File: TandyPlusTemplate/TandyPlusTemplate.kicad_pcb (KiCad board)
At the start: 2 copper layers, 3 parts, among them J1 Input BUS, J2 Passthrough Bus Short, J3 Passthrough Bus Tall

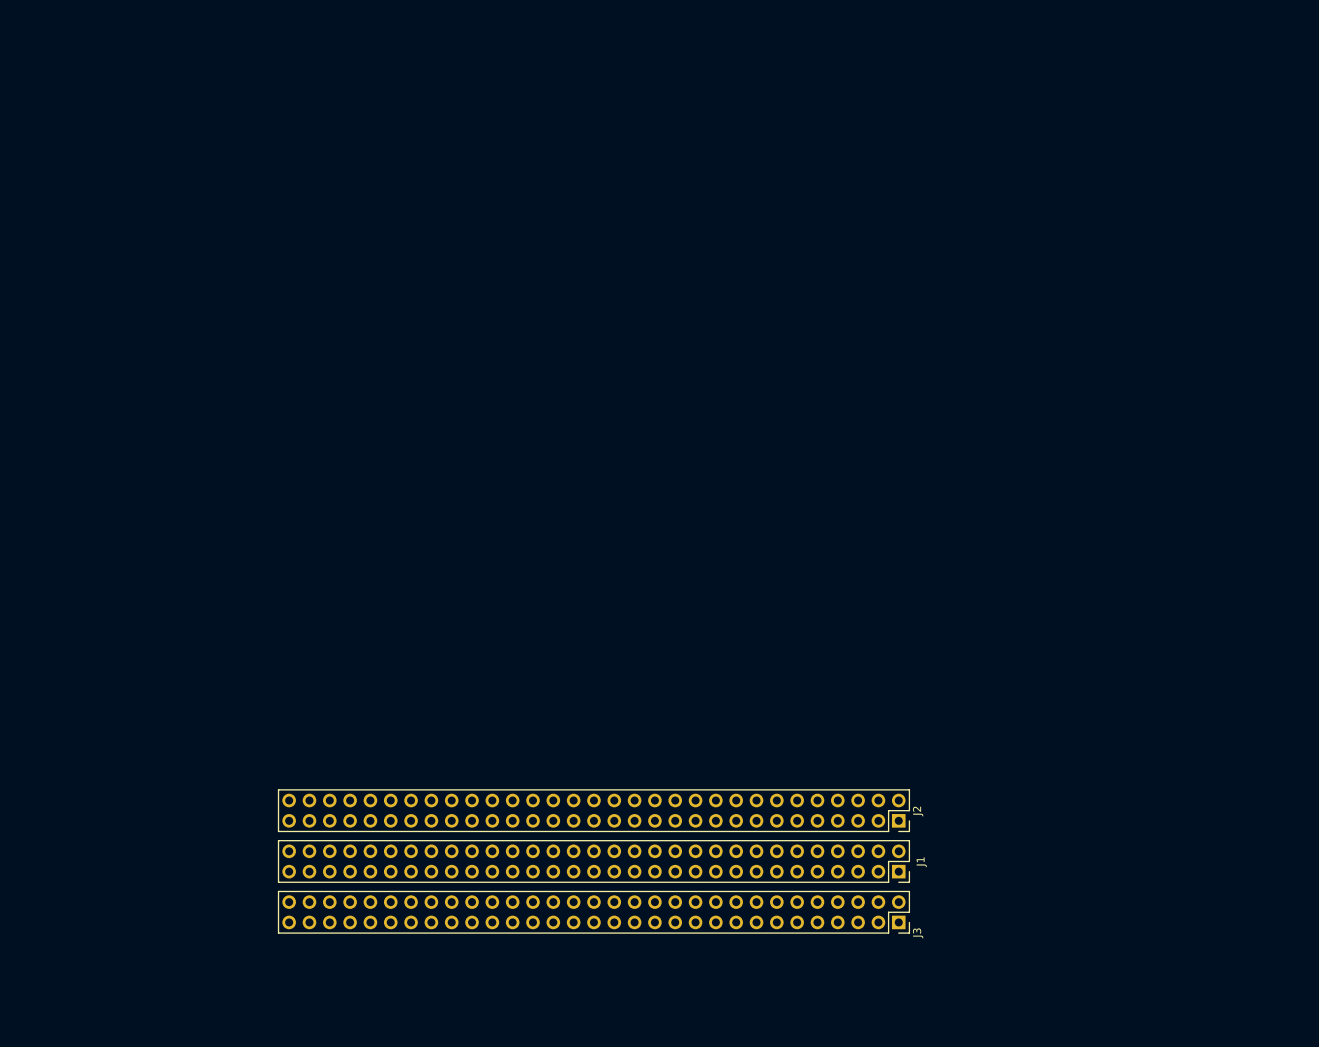
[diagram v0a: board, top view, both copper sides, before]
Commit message: Work on Tandy Plus template.
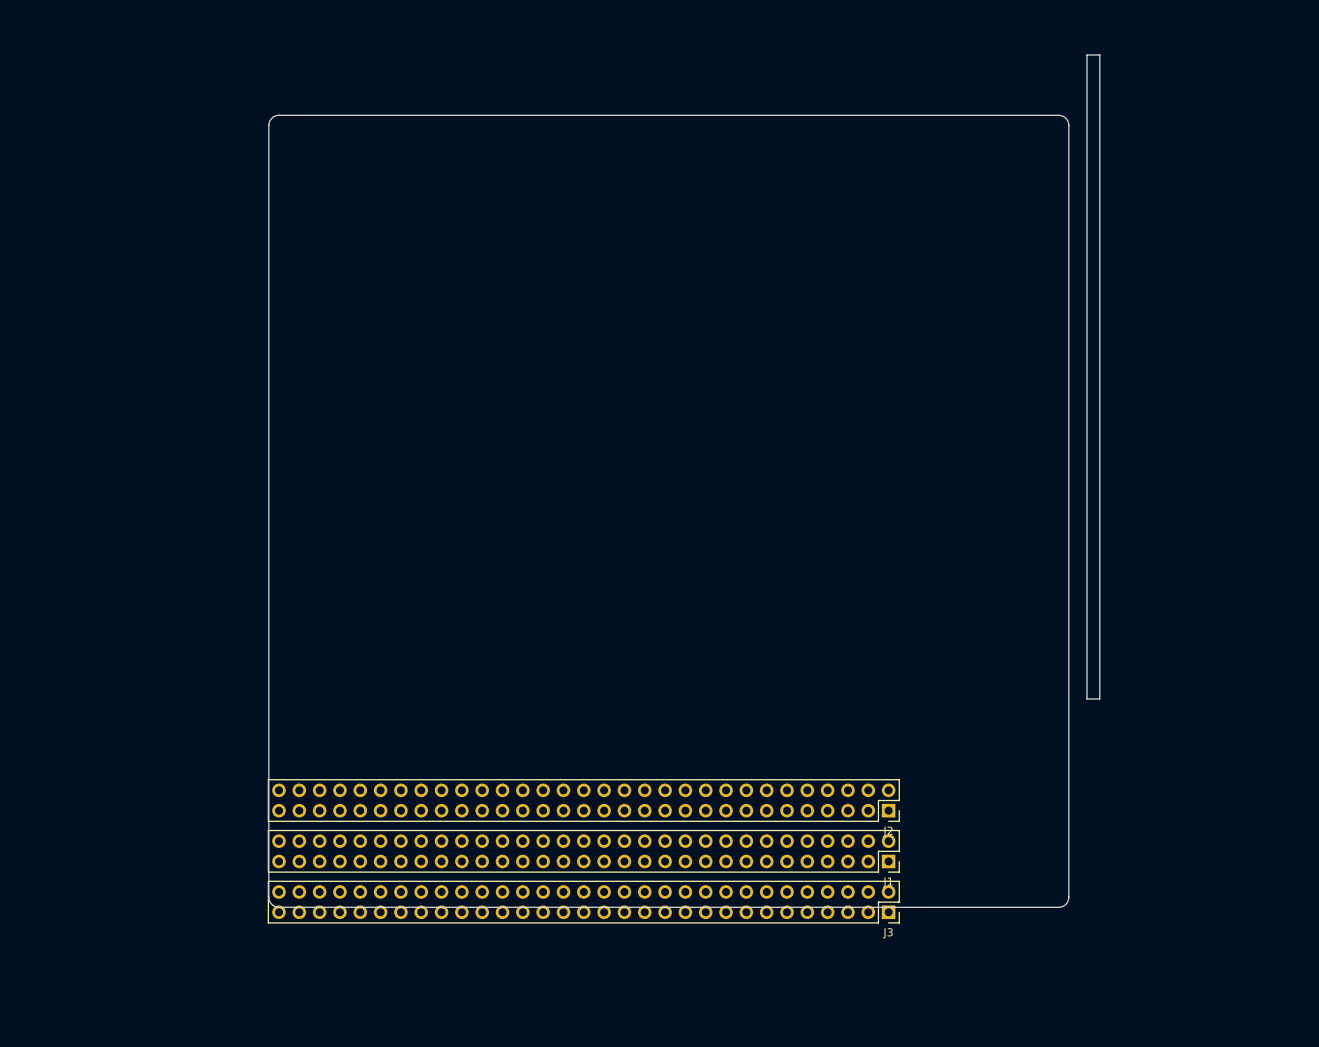
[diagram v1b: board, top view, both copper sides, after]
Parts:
- J1: footprint Connector_PinSocket_2.54mm:PinSocket_2x31_P2.54mm_Vertical -> 00Custom:TandyPlusSocket
- J2: footprint Connector_PinHeader_2.54mm:PinHeader_2x31_P2.54mm_Vertical -> 00Custom:TandyPlusShortPins
- J3: footprint Connector_PinHeader_2.54mm:PinHeader_2x31_P2.54mm_Vertical -> 00Custom:TandyPlusLongPins
- moved J1 1.80 mm to (218.4, 130.8)
- moved J2 1.80 mm to (218.4, 124.5)
- moved J3 1.80 mm to (218.4, 137.2)
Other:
- board outline added: 103.9 x 106.5 mm
- board text added: "100mm wide x 99mm high outline"
- board text added: "Rob Krenecki's 3in1 PCB outline (approx)."
- board text added: "Tandy DMA/Memory PCB outline (approx)."
- board text added: "Tandy Serial PCB outline (approx)."

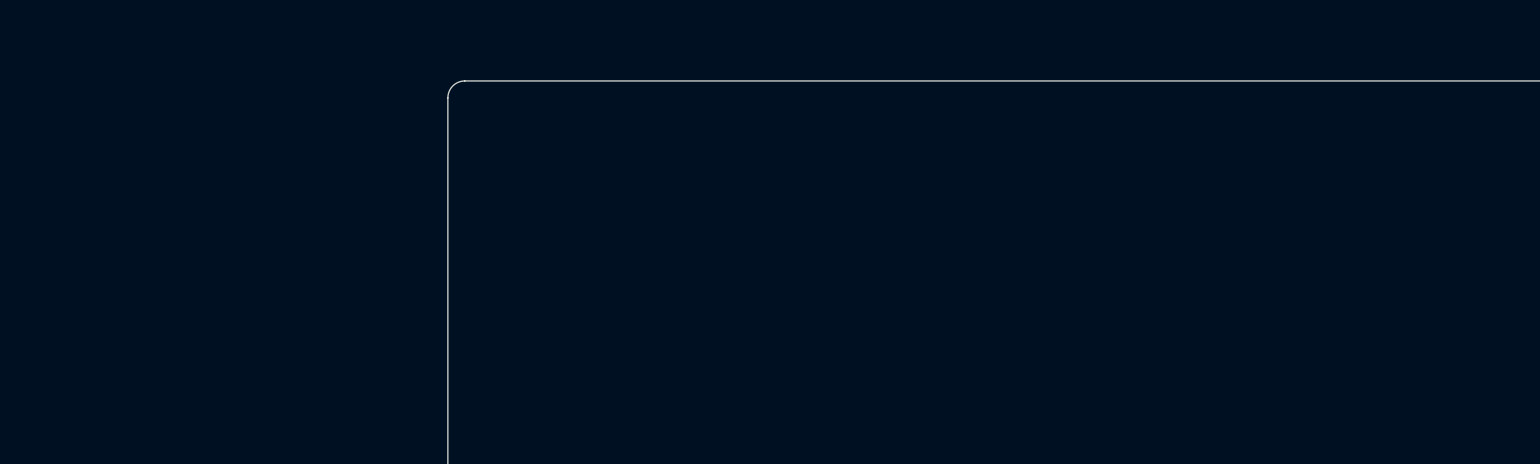
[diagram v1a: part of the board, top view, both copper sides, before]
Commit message: Additional work on Tandy Plus template.
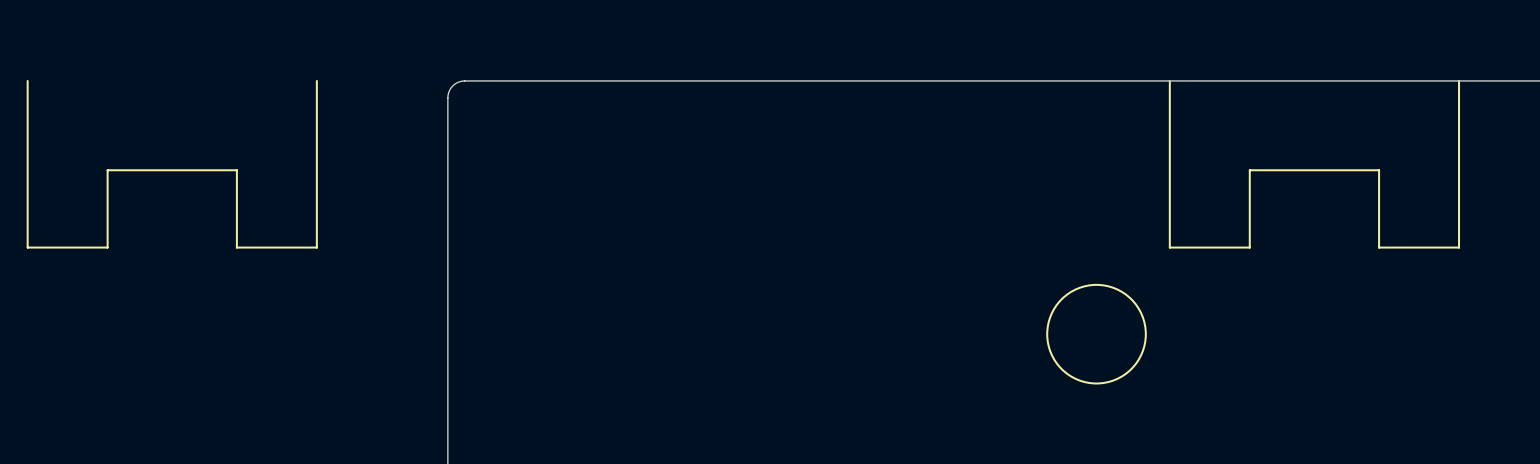
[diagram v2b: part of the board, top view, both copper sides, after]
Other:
- board text added: "Maxium recommended length. This will almost reach the ROM when a SmartWatch is fitted in an HX. Tall components this far back will hit the top of the case when the board is in the top position."
- board text added: "On the HX, there is a screw thread poking up here. It will not touch the board, however it is taller than the insulated metal shield, so avoid using any through hole pads here."
- board text added: "Safe zone for underside components. Taller components, such as DB connectors, should perhaps not be quite so close to the shield. The HX shield is sheet metal and about 2.3mm away from this line. The EX shield is floppy cardboard with foil then plastic coating. It is about 0mm away from this line and the shielding on the contacting edge may not be perfect."
- board text added: "When in the bottom board position, there is a plastic structure and screw under this area. Traces and fill will be fine within the area, however, avoid any through hole pads."

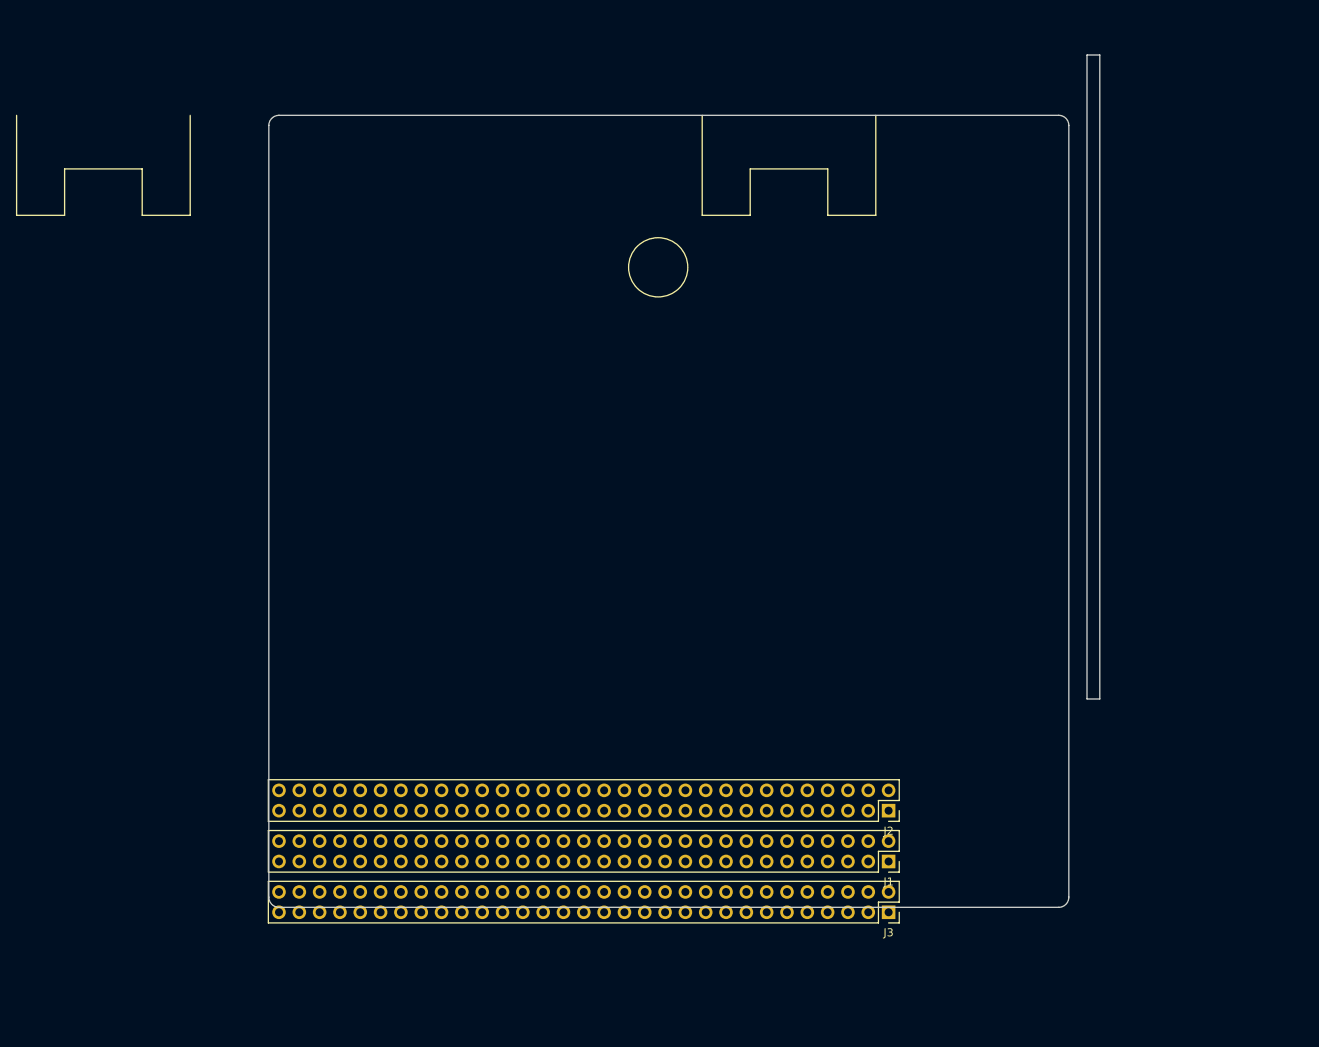
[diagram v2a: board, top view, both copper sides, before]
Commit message: Complete first pass at Tandy Plus template by adding bracket details.
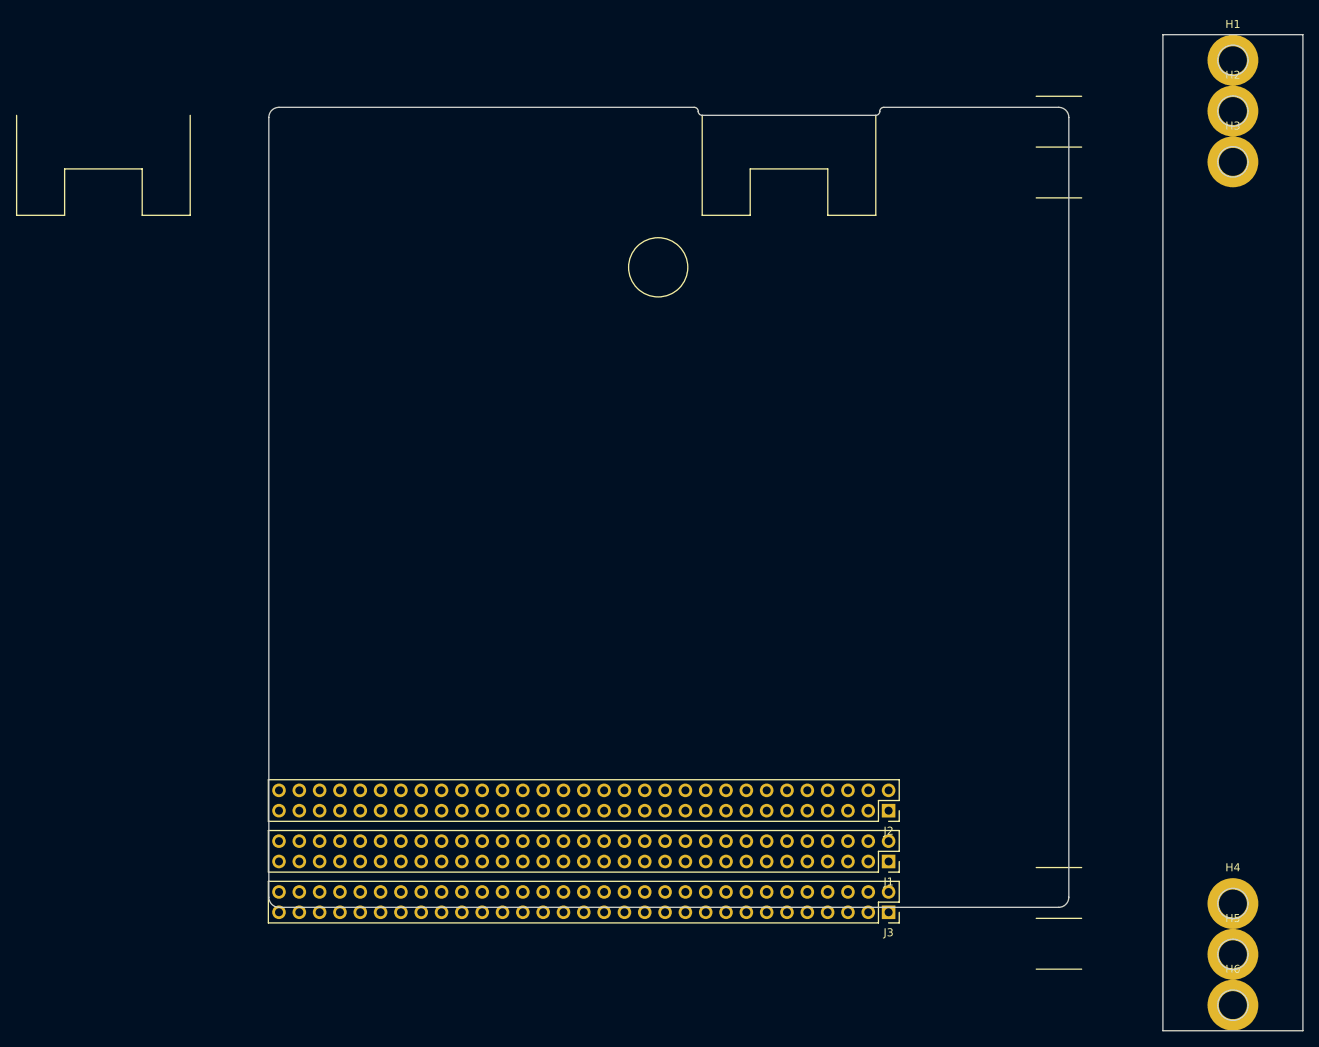
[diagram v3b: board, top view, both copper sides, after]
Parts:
- added H1: MountingHole_Pad, MountingHole:MountingHole_3.5mm_Pad, F.Cu at (261.5, 30.7)
- added H2: MountingHole_Pad, MountingHole:MountingHole_3.5mm_Pad, F.Cu at (261.5, 37.0)
- added H3: MountingHole_Pad, MountingHole:MountingHole_3.5mm_Pad, F.Cu at (261.5, 43.4)
- added H4: MountingHole_Pad, MountingHole:MountingHole_3.5mm_Pad, F.Cu at (261.5, 136.1)
- added H5: MountingHole_Pad, MountingHole:MountingHole_3.5mm_Pad, F.Cu at (261.5, 142.4)
- added H6: MountingHole_Pad, MountingHole:MountingHole_3.5mm_Pad, F.Cu at (261.5, 148.8)
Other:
- board size 103.9 x 106.5 mm -> 129.3 x 124.5 mm
- board text added: "100x100mm outline"
- board text added: "Board may extend 6mm into these voids around the board supports,"
- board text added: "These small markers show where connectors can protrude through the back plate without hitting the edge of the EX/HX case, for each of the 3 hole positions"
- board text added: "Where PCB aligns with bracket."
- board text removed: "100mm wide x 99mm high outline"
